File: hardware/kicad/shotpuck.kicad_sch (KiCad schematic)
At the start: 36 parts, among them J1 TYPE-C 6PFS 2JCB1.6-H6.7 IPX8, J2 SWD pads, Q1 DMN63D8LDW, Q2 DMN2004DWK, U1 BMD-340-A-R, U2 LSM6DSO32TR, U3 MCP73831T-2ACI/OT, U4 BQ29700DSER

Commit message: Update ShotPuck specifications and design files for USB-C integration
- Adjusted dimensions: puck diameter increased to Ø40 × 10.43 mm, with 1.6 mm free space above the cell.
- Updated IMU to ST LSM6DSO32XTR, reflecting changes in the BOM and design files.
- Revised PCB thickness from 0.8 mm to 1.2 mm, ensuring compatibility with new components.
- Enhanced layout.json and README.md to reflect the latest design specifications and assembly details.
- Removed obsolete components and updated the BOM for JLCPCB assembly.
- Regenerated fabrication files, including gerbers and BOM, to align with the latest design changes.

Co-Authored-By: Claude Opus 5.5 <noreply@anthropic.com>
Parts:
- U2: value LSM6DSO32TR -> LSM6DSO32XTR
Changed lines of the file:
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@@
 			)
 		)
-		(property "Value" "LSM6DSO32TR"
+		(property "Value" "LSM6DSO32XTR"
 			(at 227.33 210.82 0)
 			(show_name no)

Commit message: Switch U2 to LSM6DSV32XTR and assemble 4 boards
- U2 is the LSM6DSV32XTR (C22461202): same pinout and land pattern, JLC
  footprint within 0.013 mm at 0 deg. Value fields, BOMs, pos file and
  schematic PDF updated; gerbers, drill files and CPL rows unchanged.
  Board DRC 0/0 with 0 parity issues, panel DRC 0/0, ERC unchanged.
- Firmware 0.2.2: accel.c ported to the LSM6DSV32X register map. ACTIVE
  runs at 480 Hz (captures 720 samples, ring 1329, motion guard 10
  samples), IDLE at 15 Hz. Rebuilt shotpuck_full.hex and update.bin.
- Sim ground truth 3360 Hz (7 x 480 Hz); results.txt regenerated, PASS.
- JLC order: PCBA qty 2 panels, BOM/CPL for the bottom-row copies only
  (gen_jlc.py ASSEMBLED_COPIES), so 4 boards are assembled.
- README, HANDOVER, PROTOCOL, VALIDATION, ORDER.md and the order zip
  updated.

Co-Authored-By: Claude Opus 5.5 <noreply@anthropic.com>
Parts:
- U2: value LSM6DSO32XTR -> LSM6DSV32XTR
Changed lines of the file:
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@@
 		)
 	)
-	(text "design.py - ShotPuck circuit, single source of truth.\n\ngen_sch.py turns this into shotpuck.kicad_sch and gen_pcb.py into\nshotpuck.kicad_pcb. Change the circuit here, then re-run both.\n\nPower path\n  J1 USB-C power-only receptacle (VBUS = VIN_RAW) on the left rim, plug through the cap wall;\n  R10/R11 5.1k pull CC1/CC2 down so USB-C sources turn on 5 V. D3 SMF5.0CA bidirectional TVS\n  to GND (ESD, hot-plug) -> D1 BAT54J (blocks back-feed into the port) -> VIN\n  VIN -> R9 1k -> VBUS_SNS (C9 100n) -> U1 VBUS: charger detect only (USB unused, ~24 uA),\n  the RC keeps hot-plug spikes off the 5.8 V abs-max VBUS pin\n  VIN -> U3 MCP73831-2 (4.20 V, 21 mA via R1 = 47k) -> VBAT (LIR1254, 45-65 mAh)\n  VBAT -> U1 VCCH (u-blox BMD-340, nRF52840 high-voltage mode, REG0 -> VCC = VDD 3.0 V)\n  VDD  -> U2 LSM6DSO32 (VDD + VDDIO), LED, SWD VCC sense\nIMU\n  U2 LSM6DSO32 on I2C at 0x6A (SA0 = GND, CS = VDD selects I2C). Aux master\n  pins SDx/SCx to GND; INT2, OCS_Aux, SDO_Aux unconnected.\nCharge inhibit (temperature, firmware)\n  PROG -> R1 -> Q1A drain; Q1A gate pulled to VIN by R2 (charging allowed\n  whenever a cable is present). Q1B (gate = CHG_INH, R3 pull-down) pulls\n  Q1A gate low -> PROG floats -> MCP73831 charge disabled.\nCell protection (PCM; LIR cells have no protection of their own)\n  U4 BQ29700 + Q2 DMN2004DWK in the cell's negative lead: BAT_N -> Q2B (DOUT,\n  discharge) -> PCM_D -> Q2A (COUT, charge) -> GND. OVP 4.275 V, UVP 2.80 V,\n  OCD/OCC +-100 mV across ~1 ohm of FETs (~0.1 A), SCD 0.5 V. R7 330R + C8\n  100n filter the BAT supply, R8 2k2 on V-. Standby 4 uA.\nCurrent measurement\n  JP1 (bridged solder jumper) in series with the cell: cut, insert an\n  ammeter, re-bridge with solder.\nCharge status\n  STAT -> D2 (cathode) ; D2 anode -> CHG_STAT GPIO with pull-up enabled only\n  while VBUS is present (no standby leakage)."
+	(text "design.py - ShotPuck circuit, single source of truth.\n\ngen_sch.py turns this into shotpuck.kicad_sch and gen_pcb.py into\nshotpuck.kicad_pcb. Change the circuit here, then re-run both.\n\nPower path\n  J1 USB-C power-only receptacle (VBUS = VIN_RAW) on the left rim, plug through the cap wall;\n  R10/R11 5.1k pull CC1/CC2 down so USB-C sources turn on 5 V. D3 SMF5.0CA bidirectional TVS\n  to GND (ESD, hot-plug) -> D1 BAT54J (blocks back-feed into the port) -> VIN\n  VIN -> R9 1k -> VBUS_SNS (C9 100n) -> U1 VBUS: charger detect only (USB unused, ~24 uA),\n  the RC keeps hot-plug spikes off the 5.8 V abs-max VBUS pin\n  VIN -> U3 MCP73831-2 (4.20 V, 21 mA via R1 = 47k) -> VBAT (LIR1254, 45-65 mAh)\n  VBAT -> U1 VCCH (u-blox BMD-340, nRF52840 high-voltage mode, REG0 -> VCC = VDD 3.0 V)\n  VDD  -> U2 LSM6DSV32X (VDD + VDDIO), LED, SWD VCC sense\nIMU\n  U2 LSM6DSV32X on I2C at 0x6A (SA0 = GND, CS = VDD selects I2C). Aux master\n  pins SDx/SCx to GND; INT2, OCS_Aux, SDO_Aux unconnected.\nCharge inhibit (temperature, firmware)\n  PROG -> R1 -> Q1A drain; Q1A gate pulled to VIN by R2 (charging allowed\n  whenever a cable is present). Q1B (gate = CHG_INH, R3 pull-down) pulls\n  Q1A gate low -> PROG floats -> MCP73831 charge disabled.\nCell protection (PCM; LIR cells have no protection of their own)\n  U4 BQ29700 + Q2 DMN2004DWK in the cell's negative lead: BAT_N -> Q2B (DOUT,\n  discharge) -> PCM_D -> Q2A (COUT, charge) -> GND. OVP 4.275 V, UVP 2.80 V,\n  OCD/OCC +-100 mV across ~1 ohm of FETs (~0.1 A), SCD 0.5 V. R7 330R + C8\n  100n filter the BAT supply, R8 2k2 on V-. Standby 4 uA.\nCurrent measurement\n  JP1 (bridged solder jumper) in series with the cell: cut, insert an\n  ammeter, re-bridge with solder.\nCharge status\n  STAT -> D2 (cathode) ; D2 anode -> CHG_STAT GPIO with pull-up enabled only\n  while VBUS is present (no standby leakage)."
 		(exclude_from_sim no)
 		(at 22.86 228.6 0)
@@
 			)
 		)
-		(property "Value" "LSM6DSO32XTR"
+		(property "Value" "LSM6DSV32XTR"
 			(at 227.33 210.82 0)
 			(show_name no)

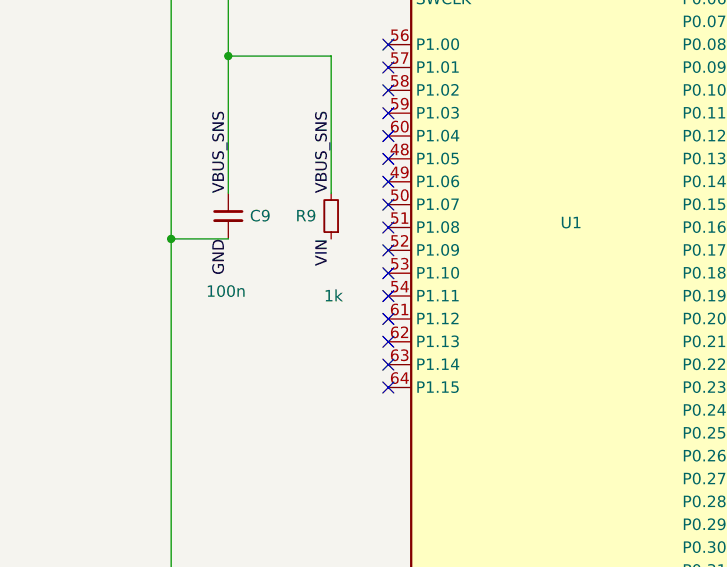
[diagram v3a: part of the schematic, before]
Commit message: Feed R9 from VIN_RAW and add the hot-plug simulation
A hot-plug simulation of the charge input (324 cases over cable,
supply, C1 derating, D1 and TVS corners) showed that D1 and C1 hold a
plug-in overshoot on VIN for milliseconds, and R9/C9 passes it on to
the nRF VBUS pin: up to 6.36 V against its 5.8 V absolute maximum in
9 cases. Fed from VIN_RAW, before D1, VBUS_SNS stays at or below
5.47 V in every case, and charger detection gains a diode drop of
headroom. R9 sat on VIN only because the magnetic board's hand-wired
lead could be reversed; a USB-C plug cannot reverse VBUS.

- design.py: R9 pin 1 on VIN_RAW.
- shotpuck.kicad_sch: R9 pin-1 label changed in place (gen_sch.py
  would drop the schematic's hand edits). Netlist check PASS, ERC 0
  errors.
- shotpuck.kicad_pcb: R9 pad 1 routed to VIN_RAW by Richard, old VIN
  branch removed. DRC 0/0, 0 schematic-parity issues.
- hardware/hotplug_sim.py: the sweep; --rev-a models the ordered
  boards, which keep R9 on VIN.
- README D27, HANDOVER and VALIDATION updated. The rev A order package
  is unchanged.

Co-Authored-By: Claude Opus 5.5 <noreply@anthropic.com>
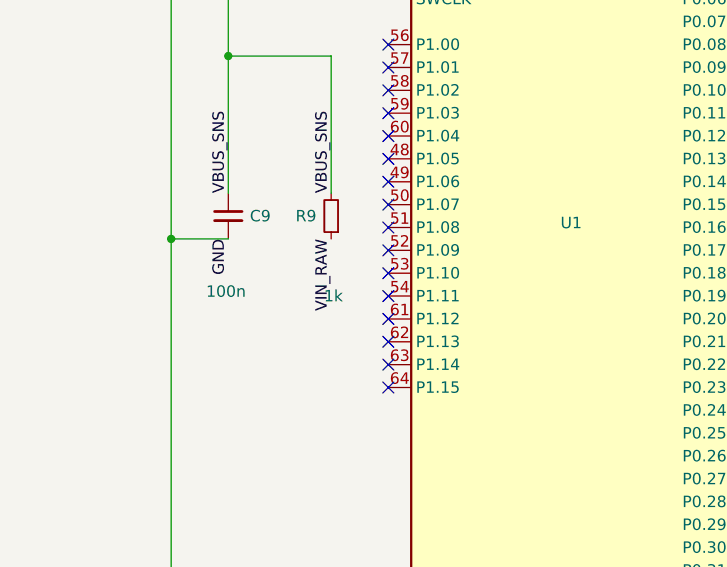
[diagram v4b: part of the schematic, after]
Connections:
- net VIN: no longer R9.1
- net VIN_RAW: now also R9.1
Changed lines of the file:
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@@
 		)
 	)
-	(label "VIN"
+	(label "VIN_RAW"
 		(at 52.07 85.09 270)
 		(effects
